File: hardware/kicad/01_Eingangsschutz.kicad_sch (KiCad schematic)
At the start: 4 parts, among them K101 G6S-2F DC5 - C16707, Q111 DMN2056U-7

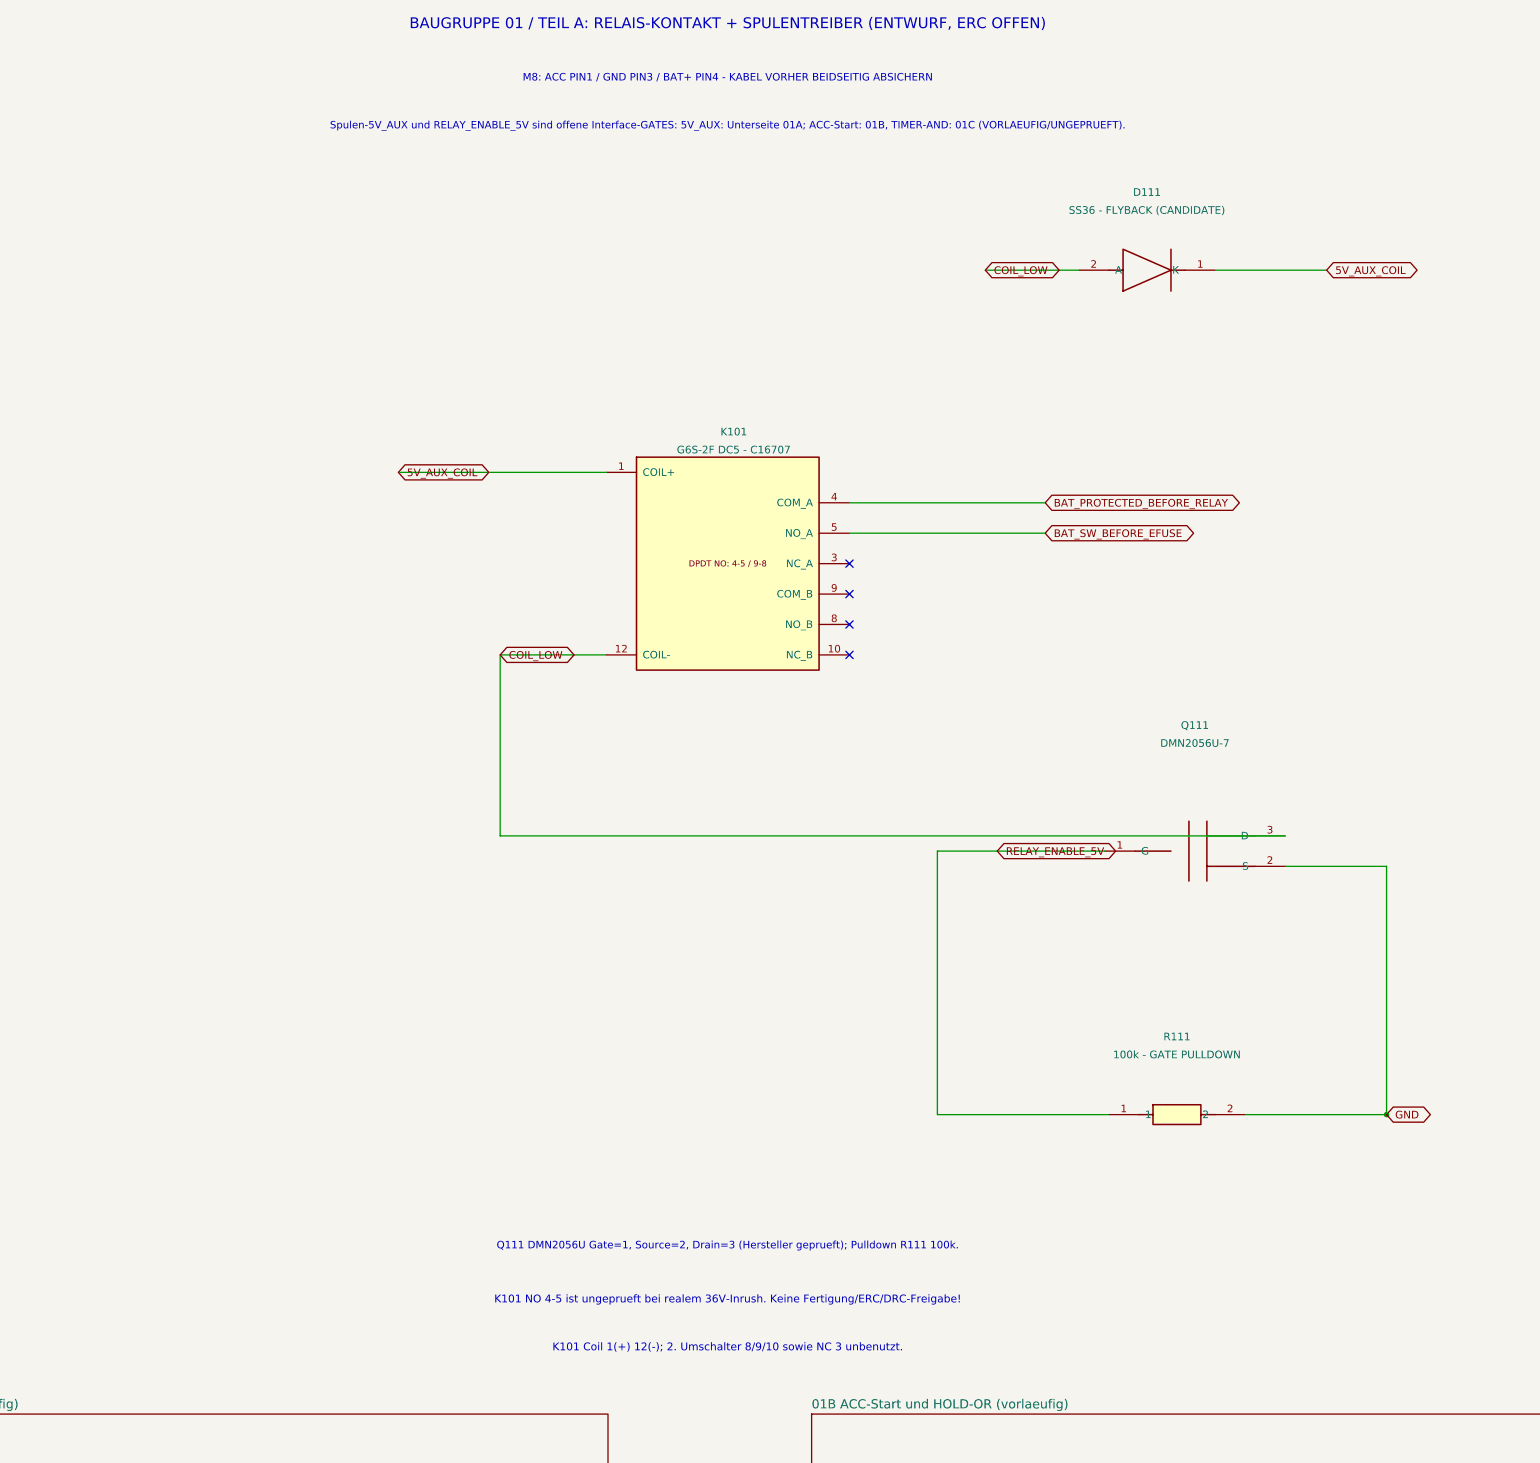
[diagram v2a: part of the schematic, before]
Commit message: hardware(kicad): remove obsolete relay K101 power stage while preserving all six input sub-sheets
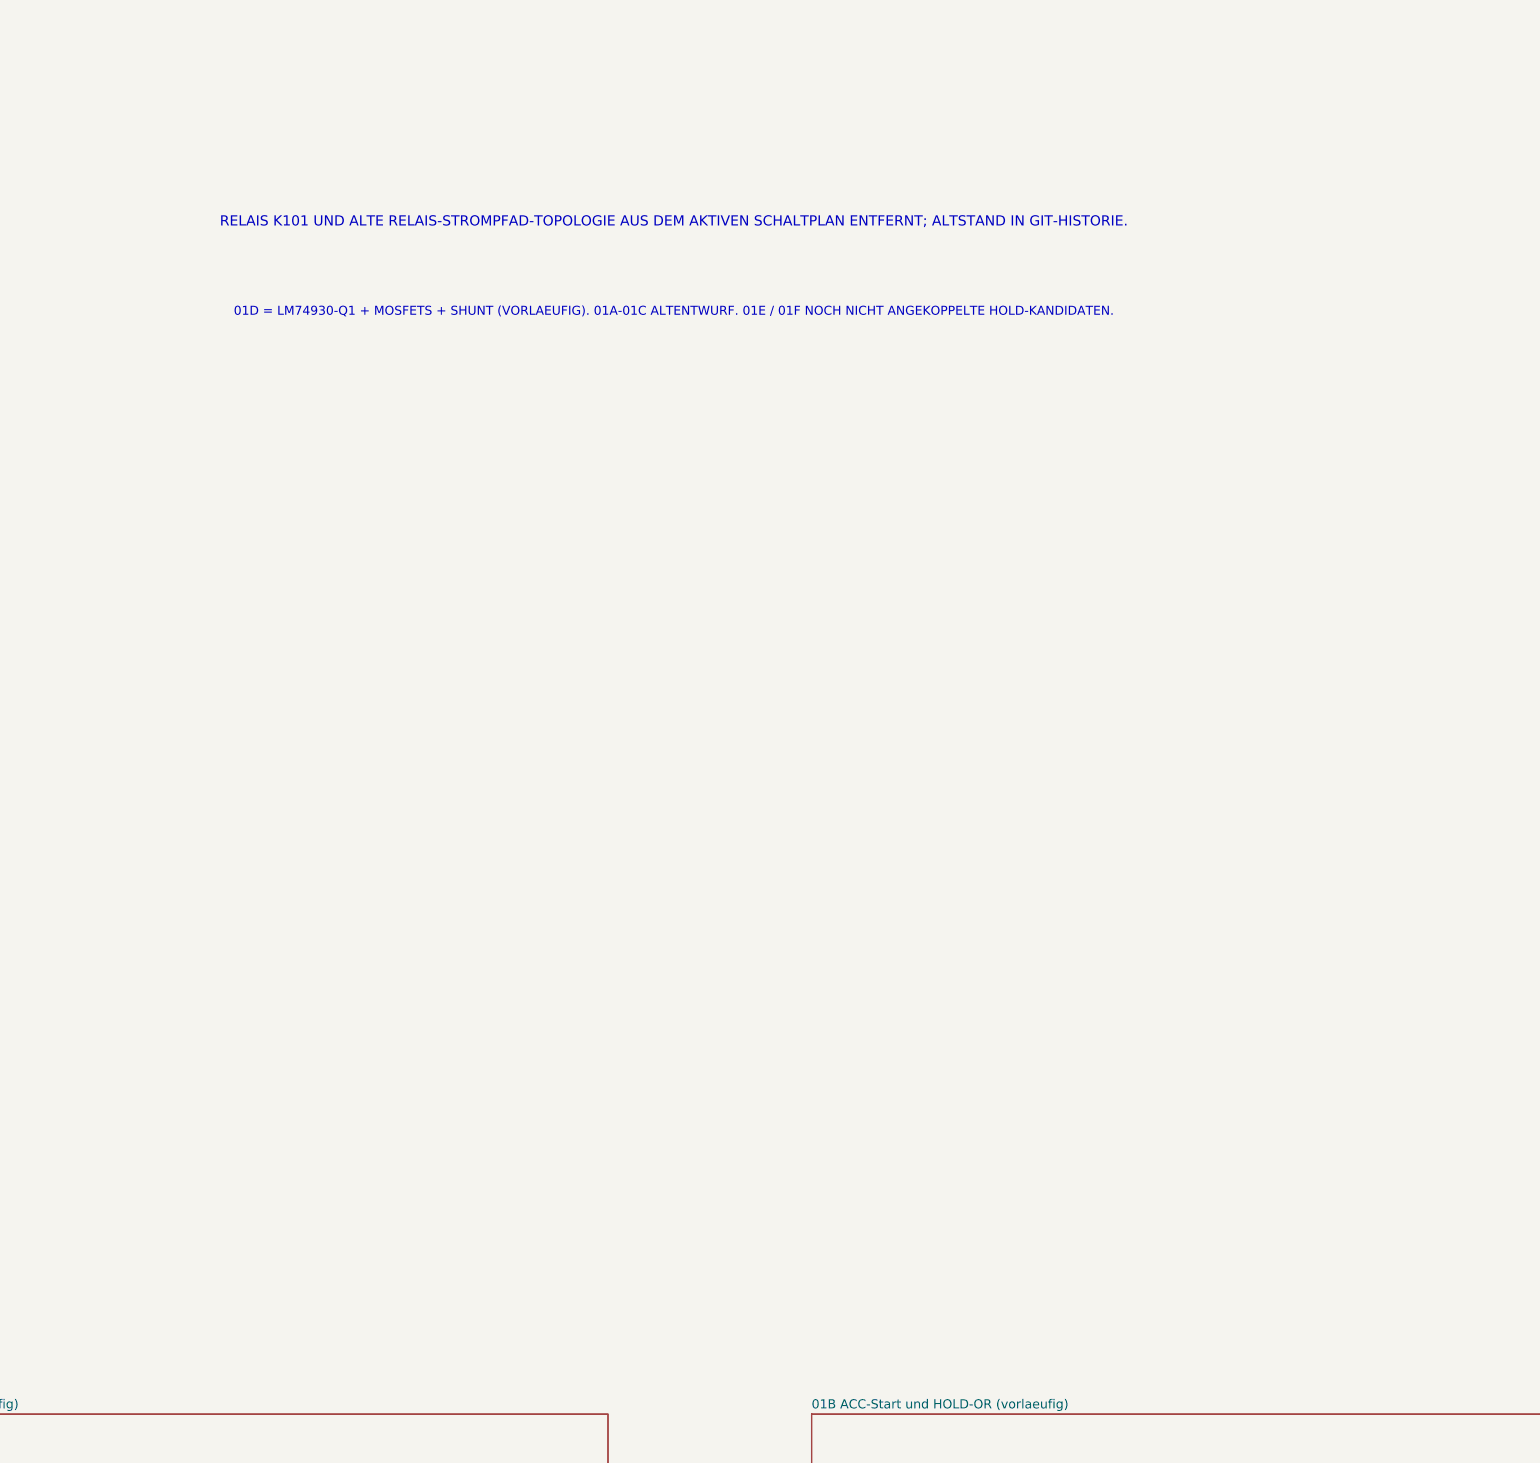
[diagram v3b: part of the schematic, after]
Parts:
- removed D111: SS36 - FLYBACK (CANDIDATE), Tripmaster:D_SMA_SS36, symbol Tripmaster_Sym:SCHOTTKY
- removed K101: G6S-2F DC5 - C16707, Tripmaster:RLY101_Omron_G6S_2F, symbol TripTracer_V1:G6S_2F_DC5
- removed Q111: DMN2056U-7, Tripmaster:Q1_Diodes_DMN2056U_7, symbol Tripmaster_Sym:NMOS
- removed R111: 100k - GATE PULLDOWN, Tripmaster:R_1206_3216, symbol Tripmaster_Sym:R
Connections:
- no-connect marks 4 -> 0
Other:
- note added: "01D = LM74930-Q1 + MOSFETS + SHUNT (VORLAEUFIG). 01A-01C ALTENTWURF. 01E / 01F NOCH NICHT ANGEKOPPELTE HOLD-KANDIDATEN."
- note added: "RELAIS K101 UND ALTE RELAIS-STROMPFAD-TOPOLOGIE AUS DEM AKTIVEN SCHALTPLAN ENTFERNT; ALTSTAND IN GIT-HISTORIE."
- note removed: "BAUGRUPPE 01 / TEIL A: RELAIS-KONTAKT + SPULENTREIBER (ENTWURF, ERC OFFEN)"
- note removed: "K101 Coil 1(+) 12(-); 2. Umschalter 8/9/10 sowie NC 3 unbenutzt."
- note removed: "K101 NO 4-5 ist ungeprueft bei realem 36V-Inrush. Keine Fertigung/ERC/DRC-Freigabe!"
- note removed: "M8: ACC PIN1 / GND PIN3 / BAT+ PIN4 - KABEL VORHER BEIDSEITIG ABSICHERN"
- note removed: "Q111 DMN2056U Gate=1, Source=2, Drain=3 (Hersteller geprueft); Pulldown R111 100k."
- note removed: "Spulen-5V_AUX und RELAY_ENABLE_5V sind offene Interface-GATES: 5V_AUX: Unterseite 01A; ACC-Start: 01B, TIMER-AND: 01C (VORLAEUFIG/UNGEPRUEFT)."
- title: TripTracer V1 - ACC/BAT+ Eingangsschutz und Relais -> TripTracer V1 - Automotive Eingangsschutz, relayless design
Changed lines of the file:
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@@
 (kicad_sch (version 20250114) (generator "eeschema")
- (paper "A2")
- (title_block (title "TripTracer V1 - ACC/BAT+ Eingangsschutz und Relais") (date "2026-10-13") (rev "a1 / RELAIS-TEILENTWURF - NICHT ERC-GEPRUEFT"))
- (symbol (lib_id "TripTracer_V1:G6S_2F_DC5") (at 200 115 0) (unit 1) (exclude_from_sim no) (in_bom yes) (on_board yes) (dnp no)
- (property "Reference" "K101" (at 201 93 0) (effects (font (size 1.27 1.27))))
- (property "Value" "G6S-2F DC5 - C16707" (at 201 96 0) (effects (font (size 1.27 1.27))))
- (property "Footprint" "Tripmaster:RLY101_Omron_G6S_2F" (at 200 115 0) (effects (font (size 1.27 1.27)) (hide yes)))
- (pin "1") (pin "12") (pin "4") (pin "5") (pin "3") (pin "9") (pin "8") (pin "10")
- (instances (project "TripTracer_V1" (path "/a26d9b0c-7f10-4e5a-a65f-000000000064/a26d9b0c-7f10-4e5a-a65f-000000000065" (reference "K101") (unit 1)))))
-(symbol (lib_id "Tripmaster_Sym:NMOS") (at 278 163 0) (unit 1) (exclude_from_sim no) (in_bom yes) (on_board yes) (dnp no)
- (property "Reference" "Q111" (at 278 142 0) (effects (font (size 1.27 1.27))))
- (property "Value" "DMN2056U-7" (at 278 145 0) (effects (font (size 1.27 1.27))))
- (property "Footprint" "Tripmaster:Q1_Diodes_DMN2056U_7" (at 278 163 0) (effects (font (size 1.27 1.27)) (hide yes)))
- (pin "1") (pin "2") (pin "3")
- (instances (project "TripTracer_V1" (path "/a26d9b0c-7f10-4e5a-a65f-000000000064/a26d9b0c-7f10-4e5a-a65f-000000000065" (reference "Q111") (unit 1)))))
-(symbol (lib_id "Tripmaster_Sym:SCHOTTKY") (at 270 66 0) (unit 1) (exclude_from_sim no) (in_bom yes) (on_board yes) (dnp no)
- (property "Reference" "D111" (at 270 53 0) (effects (font (size 1.27 1.27))))
- (property "Value" "SS36 - FLYBACK (CANDIDATE)" (at 270 56 0) (effects (font (size 1.27 1.27))))
- (property "Footprint" "Tripmaster:D_SMA_SS36" (at 270 66 0) (effects (font (size 1.27 1.27)) (hide yes)))
- (pin "1") (pin "2")
- (instances (project "TripTracer_V1" (path "/a26d9b0c-7f10-4e5a-a65f-000000000064/a26d9b0c-7f10-4e5a-a65f-000000000065" (reference "D111") (unit 1)))))
-(symbol (lib_id "Tripmaster_Sym:R") (at 275 207 0) (unit 1) (exclude_from_sim no) (in_bom yes) (on_board yes) (dnp no)
- (property "Reference" "R111" (at 275 194 0) (effects (font (size 1.27 1.27))))
- (property "Value" "100k - GATE PULLDOWN" (at 275 197 0) (effects (font (size 1.27 1.27))))
- (property "Footprint" "Tripmaster:R_1206_3216" (at 275 207 0) (effects (font (size 1.27 1.27)) (hide yes)))
- (pin "1") (pin "2")
- (instances (project "TripTracer_V1" (path "/a26d9b0c-7f10-4e5a-a65f-000000000064/a26d9b0c-7f10-4e5a-a65f-000000000065" (reference "R111") (unit 1)))))
- (wire (pts (xy 145 99.76) (xy 179.68 99.76)) (stroke (width 0) (type default)))
-(global_label "5V_AUX_COIL" (shape bidirectional) (at 145 99.76 0) (effects (font (size 1.27 1.27)) (justify left)))
-(wire (pts (xy 179.68 130.24) (xy 162 130.24)) (stroke (width 0) (type default)))
-(wire (pts (xy 162 130.24) (xy 162 160.46)) (stroke (width 0) (type default)))
-(wire (pts (xy 162 160.46) (xy 293.08 160.46)) (stroke (width 0) (type default)))
-(global_label "COIL_LOW" (shape bidirectional) (at 162 130.24 0) (effects (font (size 1.27 1.27)) (justify left)))
-(wire (pts (xy 220.32 104.84) (xy 253 104.84)) (stroke (width 0) (type default)))
-(global_label "BAT_PROTECTED_BEFORE_RELAY" (shape bidirectional) (at 253 104.84 0) (effects (font (size 1.27 1.27)) (justify left)))
-(wire (pts (xy 220.32 109.92) (xy 253 109.92)) (stroke (width 0) (type default)))
-(global_label "BAT_SW_BEFORE_EFUSE" (shape bidirectional) (at 253 109.92 0) (effects (font (size 1.27 1.27)) (justify left)))
-(no_connect (at 220.32 115))
-(no_connect (at 220.32 120.08))
-(no_connect (at 220.32 125.16))
-(no_connect (at 220.32 130.24))
-(wire (pts (xy 293.08 165.54) (xy 310 165.54)) (stroke (width 0) (type default)))
-(wire (pts (xy 310 165.54) (xy 310 207)) (stroke (width 0) (type default)))
-(global_label "GND" (shape bidirectional) (at 310 207 0) (effects (font (size 1.27 1.27)) (justify left)))
-(wire (pts (xy 262.92 163) (xy 245 163)) (stroke (width 0) (type default)))
-(global_label "RELAY_ENABLE_5V" (shape bidirectional) (at 245 163 0) (effects (font (size 1.27 1.27)) (justify left)))
-(wire (pts (xy 245 163) (xy 235 163)) (stroke (width 0) (type default)))
-(wire (pts (xy 235 163) (xy 235 207)) (stroke (width 0) (type default)))
-(wire (pts (xy 235 207) (xy 263.57 207)) (stroke (width 0) (type default)))
-(wire (pts (xy 286.43 207) (xy 310 207)) (stroke (width 0) (type default)))
-(junction (at 310 207) (diameter 0) (color 0 0 0 0))
-(wire (pts (xy 243 66) (xy 258.57 66)) (stroke (width 0) (type default)))
-(global_label "COIL_LOW" (shape bidirectional) (at 243 66 0) (effects (font (size 1.27 1.27)) (justify left)))
-(wire (pts (xy 281.43 66) (xy 300 66)) (stroke (width 0) (type default)))
-(global_label "5V_AUX_COIL" (shape bidirectional) (at 300 66 0) (effects (font (size 1.27 1.27)) (justify left)))
-(text "BAUGRUPPE 01 / TEIL A: RELAIS-KONTAKT + SPULENTREIBER (ENTWURF, ERC OFFEN)" (at 200 25 0) (effects (font (size 1.8 1.8))))
-(text "M8: ACC PIN1 / GND PIN3 / BAT+ PIN4 - KABEL VORHER BEIDSEITIG ABSICHERN" (at 200 34 0) (effects (font (size 1.25 1.25))))
-(text "Spulen-5V_AUX und RELAY_ENABLE_5V sind offene Interface-GATES: 5V_AUX: Unterseite 01A; ACC-Start: 01B, TIMER-AND: 01C (VORLAEUFIG/UNGEPRUEFT)." (at 200 42 0) (effects (font (size 1.23 1.23))))
-(text "Q111 DMN2056U Gate=1, Source=2, Drain=3 (Hersteller geprueft); Pulldown R111 100k." (at 200 229 0) (effects (font (size 1.25 1.25))))
-(text "K101 NO 4-5 ist ungeprueft bei realem 36V-Inrush. Keine Fertigung/ERC/DRC-Freigabe!" (at 200 238 0) (effects (font (size 1.3 1.3))))
-(text "K101 Coil 1(+) 12(-); 2. Umschalter 8/9/10 sowie NC 3 unbenutzt." (at 200 246 0) (effects (font (size 1.3 1.3))))
- (sheet (at 25 257) (size 155 28) (exclude_from_sim no) (in_bom yes) (on_board yes) (dnp no)
+(paper "A2")
+(title_block (title "TripTracer V1 - Automotive Eingangsschutz, relayless design") (date "2026-10-14") (rev "RELAY REMOVED / LM74930+LMR36520 WIP"))
+(text "RELAIS K101 UND ALTE RELAIS-STROMPFAD-TOPOLOGIE AUS DEM AKTIVEN SCHALTPLAN ENTFERNT; ALTSTAND IN GIT-HISTORIE." (at 191 58 0) (effects (font (size 1.7 1.7))))
+(text "01D = LM74930-Q1 + MOSFETS + SHUNT (VORLAEUFIG). 01A-01C ALTENTWURF. 01E / 01F NOCH NICHT ANGEKOPPELTE HOLD-KANDIDATEN." (at 191 73 0) (effects (font (size 1.5 1.5))))
+(sheet (at 25 257) (size 155 28) (exclude_from_sim no) (in_bom yes) (on_board yes) (dnp no)
  (stroke (width 0) (type solid)) (fill (color 0 0 0 0))
  (property "Sheetname" "01A Hilfsversorgung - LM5164-Q1 5V AUX (vorlaeufig)" (at 25 256.24 0) (effects (font (size 1.524 1.524)) (justify left bottom)))
@@
  (instances (project "TripTracer_V1" (path "/a26d9b0c-7f10-4e5a-a65f-000000000064/a26d9b0c-7f10-4e5a-a65f-000000000065" (page "2.1"))))
 )
- (sheet (at 214 257) (size 175 28) (exclude_from_sim no) (in_bom yes) (on_board yes) (dnp no)
+(sheet (at 214 257) (size 175 28) (exclude_from_sim no) (in_bom yes) (on_board yes) (dnp no)
  (stroke (width 0) (type solid)) (fill (color 0 0 0 0))
  (property "Sheetname" "01B ACC-Start und HOLD-OR (vorlaeufig)" (at 214 256.24 0) (effects (font (size 1.524 1.524)) (justify left bottom)))
@@
  (instances (project "TripTracer_V1" (path "/a26d9b0c-7f10-4e5a-a65f-000000000064/a26d9b0c-7f10-4e5a-a65f-000000000065" (page "2.4"))))
 )
- (sheet (at 25 328.93) (size 185.42 27.94) (exclude_from_sim no) (in_bom yes) (on_board yes) (dnp no)
+(sheet (at 25 328.93) (size 185.42 27.94) (exclude_from_sim no) (in_bom yes) (on_board yes) (dnp no)
  (stroke (width 0) (type solid)) (fill (color 0 0 0 0))
  (property "Sheetname" "01E ACC-OFF hardware latch (isolierter Vorentwurf)" (at 25 328.17 0) (effects (font (size 1.524 1.524)) (justify left bottom)))
@@
 )
 (sheet_instances (path "/" (page "2")))
- (embedded_fonts no)
+(embedded_fonts no)
 )
